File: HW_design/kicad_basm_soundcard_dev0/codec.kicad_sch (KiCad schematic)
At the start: 44 parts, among them J401 AudioJack3, J402 AudioJack3, U401 ES8388

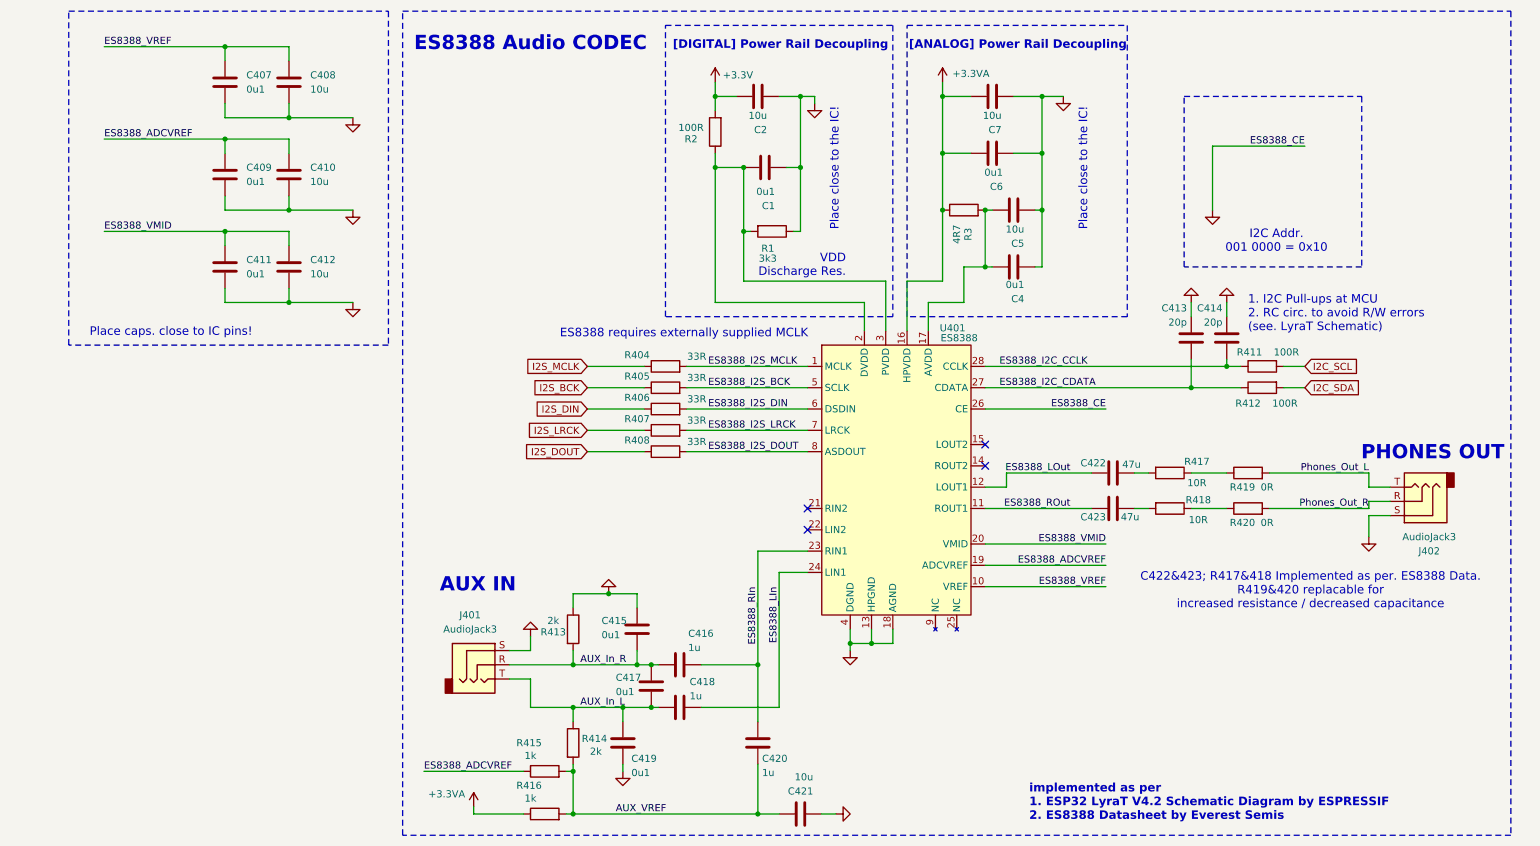
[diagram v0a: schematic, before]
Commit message: Changed Footprints for LED RGB, SD, AudioJack, USB
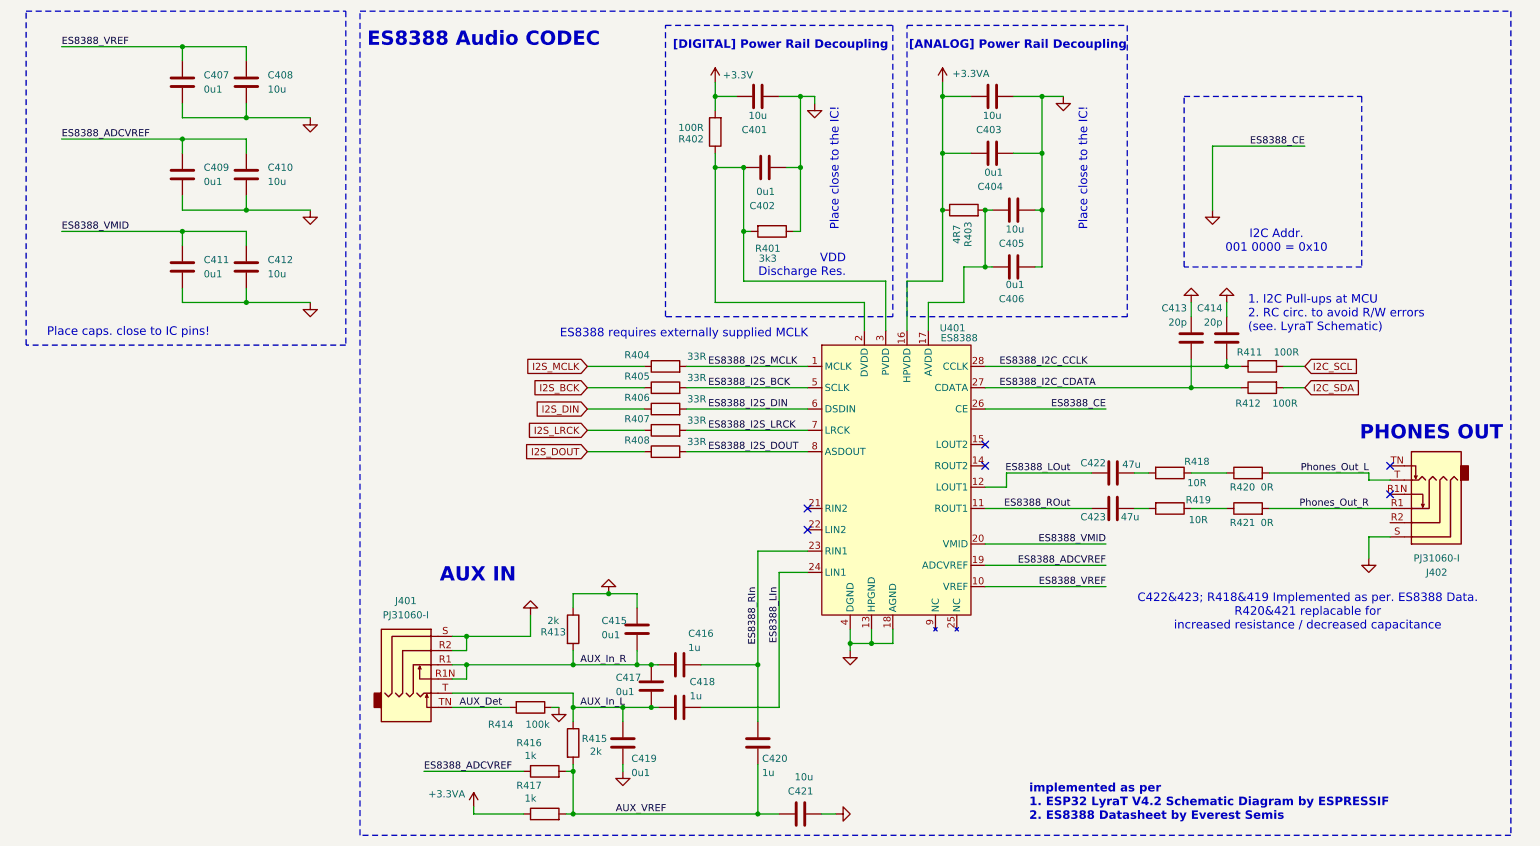
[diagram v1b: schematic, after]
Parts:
- removed J401, J402: AudioJack3, Connector_Audio:Jack_3.5mm_CUI_SJ-3523-SMT_Horizontal, symbol Connector_Audio:AudioJack3
- added J401, J402: PJ31060-I, Connector_Audio:Jack_3.5mm_PJ31060-I_Horizontal, symbol Connector_Audio:AudioJack4_SwitchTR1
- added R414: 100k, Resistor_SMD:R_0402_1005Metric, symbol Device:R
- C401: renamed from C2; footprint Capacitor_SMD:C_0402_1005Metric -> Capacitor_SMD:C_0603_1608Metric
- C403: renamed from C7; footprint Capacitor_SMD:C_0402_1005Metric -> Capacitor_SMD:C_0603_1608Metric
- C405: renamed from C5; footprint Capacitor_SMD:C_0402_1005Metric -> Capacitor_SMD:C_0603_1608Metric
- C408, C410, C412, C421: footprint Capacitor_SMD:C_0402_1005Metric -> Capacitor_SMD:C_0603_1608Metric
- renumbered C1 to C402, C6 to C404, C4 to C406, R1 to R401, R2 to R402, R3 to R403, R414 to R415, R415 to R416, R416 to R417, R417 to R418, R418 to R419, R419 to R420, R420 to R421
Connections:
- net AUX_In_L: now also J401.T
- net AUX_In_R: now also J401.R1, J401.R1N
- net GND: now also J401.R2, J401.S, J402.S, R414.1
- net Phones_Out_L: now also J402.T
- net Phones_Out_R: now also J402.R1
- new net AUX_Det: J401.TN, R414.2
- no-connect marks 4 -> 6
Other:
- note added: "C422&423; R418&419 Implemented as per. ES8388 Data. R420&421 replacable for increased resistance / decreased capacitance"
- note removed: "C422&423; R417&418 Implemented as per. ES8388 Data. R419&420 replacable for increased resistance / decreased capacitance"
- company: (none) -> BUCHAREST APPLIED STEAM MUSEUM
- title: (none) -> BASM SOUNDCARD
- moved on the sheet: C407, C408, C409, C410, C411, C412
